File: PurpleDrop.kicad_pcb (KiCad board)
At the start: 4 copper layers, 213 x 141 mm, 118 parts, among them J1 Conn_02x32_Odd_Even, J2 Conn_02x32_Odd_Even, J3 Conn_02x20_Odd_Even, J4 Conn_01x04, J5 Conn_01x04, J6 Conn_01x04, J7 Conn_02x04_Odd_Even, J8 Conn_02x10_Odd_Even, J9 Barrel_Jack_Switch, Q1 SSM3K329R, Q2 SSM3K329R, Q3 SSM3K329R, Q4 SSM3K329R, U1 HV507, U10 RRE04EA6DFH, U11 RRE04EA6DFH, U12 RRE04EA6DFH, U13 RRE04EA6DFH, U14 RRE04EA6DFH, U15 RRE04EA6DFH, U16 RRE04EA6DFH, U17 RRE04EA6DFH, U18 RRE04EA6DFH, U19 RRE04EA6DFH, U2 HV507, U20 RRE04EA6DFH, U21 RRE04EA6DFH, U22 RRE04EA6DFH, U23 RRE04EA6DFH, U24 RRE04EA6DFH, U25 RRE04EA6DFH, U26 RRE04EA6DFH, U27 RRE04EA6DFH, U28 RRE04EA6DFH, U29 RRE04EA6DFH, U3 RRE04EA6DFH, U30 RRE04EA6DFH, U31 RRE04EA6DFH, U32 RRE04EA6DFH, U33 RRE04EA6DFH, U34 RRE04EA6DFH, U35 RRE04EA6DFH, U36 RRE04EA6DFH, U37 RRE04EA6DFH, U38 RRE04EA6DFH, U39 RRE04EA6DFH, U4 RRE04EA6DFH, U40 RRE04EA6DFH, U41 RRE04EA6DFH, U42 RRE04EA6DFH, U43 RRE04EA6DFH, U44 RRE04EA6DFH, U45 RRE04EA6DFH, U46 RRE04EA6DFH, U47 RRE04EA6DFH, U48 RRE04EA6DFH, U49 RRE04EA6DFH, U5 RRE04EA6DFH, U50 RRE04EA6DFH, U51 RRE04EA6DFH, U52 RRE04EA6DFH, U53 RRE04EA6DFH, U54 RRE04EA6DFH, U55 RRE04EA6DFH, U56 RRE04EA6DFH, U57 RRE04EA6DFH, U58 RRE04EA6DFH, U59 RRE04EA6DFH, U6 RRE04EA6DFH, U60 RRE04EA6DFH, U61 RRE04EA6DFH, U62 RRE04EA6DFH, U63 RRE04EA6DFH, U64 RRE04EA6DFH, U65 RRE04EA6DFH, U66 RRE04EA6DFH, U67 74LVC2T45DCT, U68 74LVC2T45DCT, U69 74LVC2T45DCT, U7 RRE04EA6DFH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

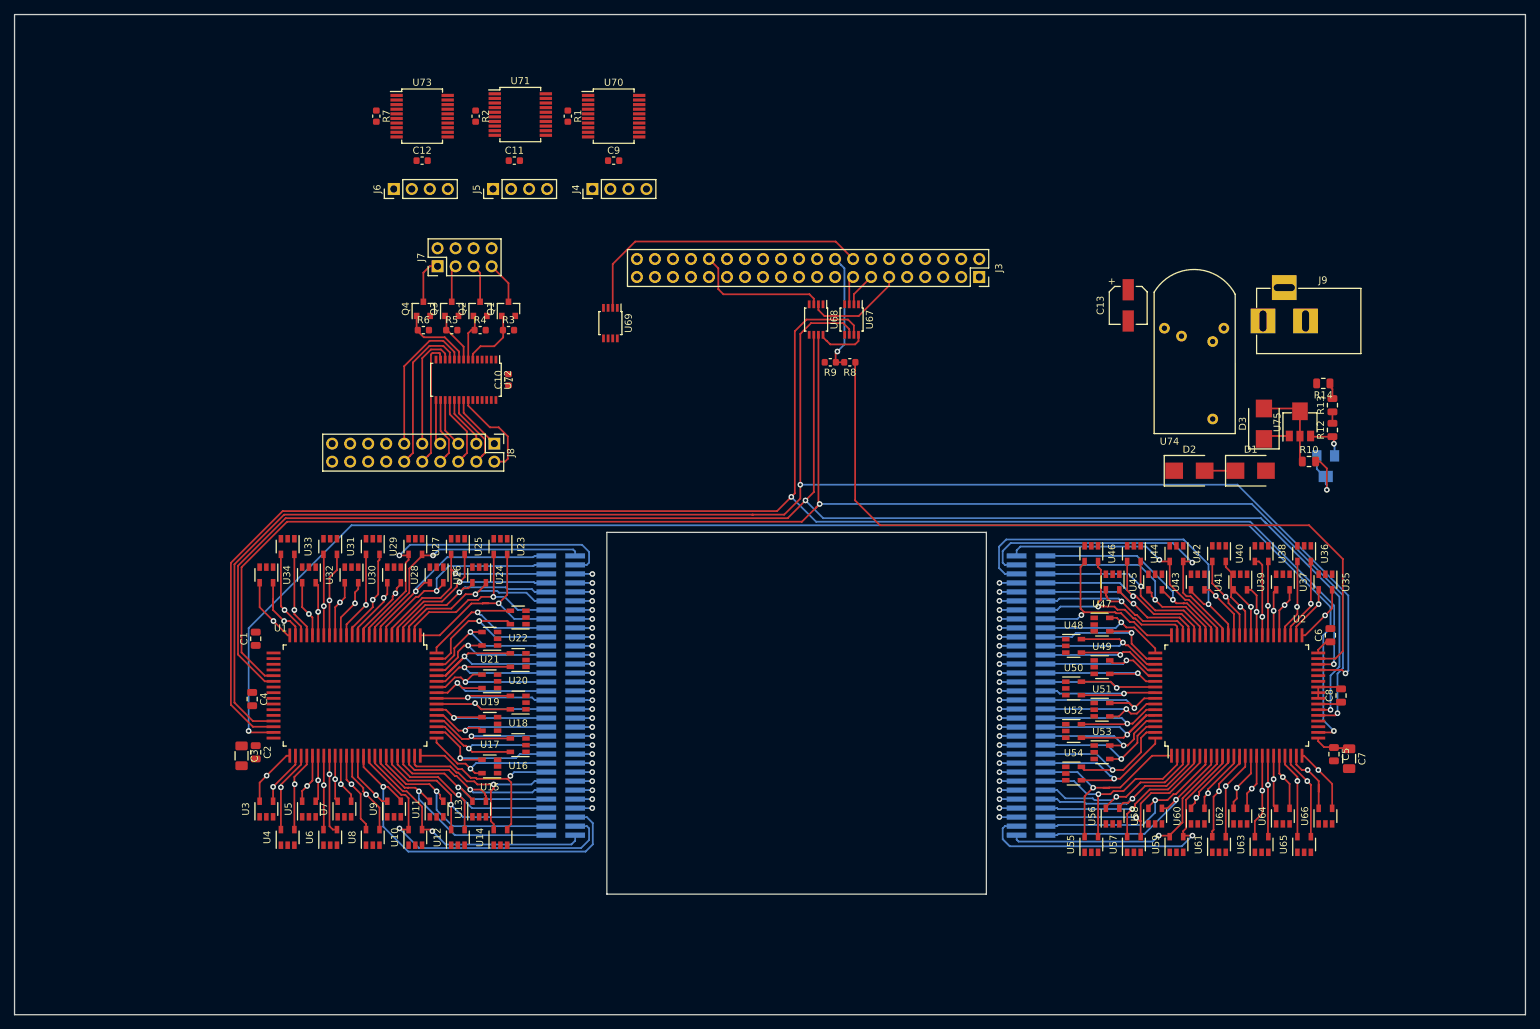
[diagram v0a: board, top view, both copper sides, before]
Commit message: feature complete.  need silk modifications
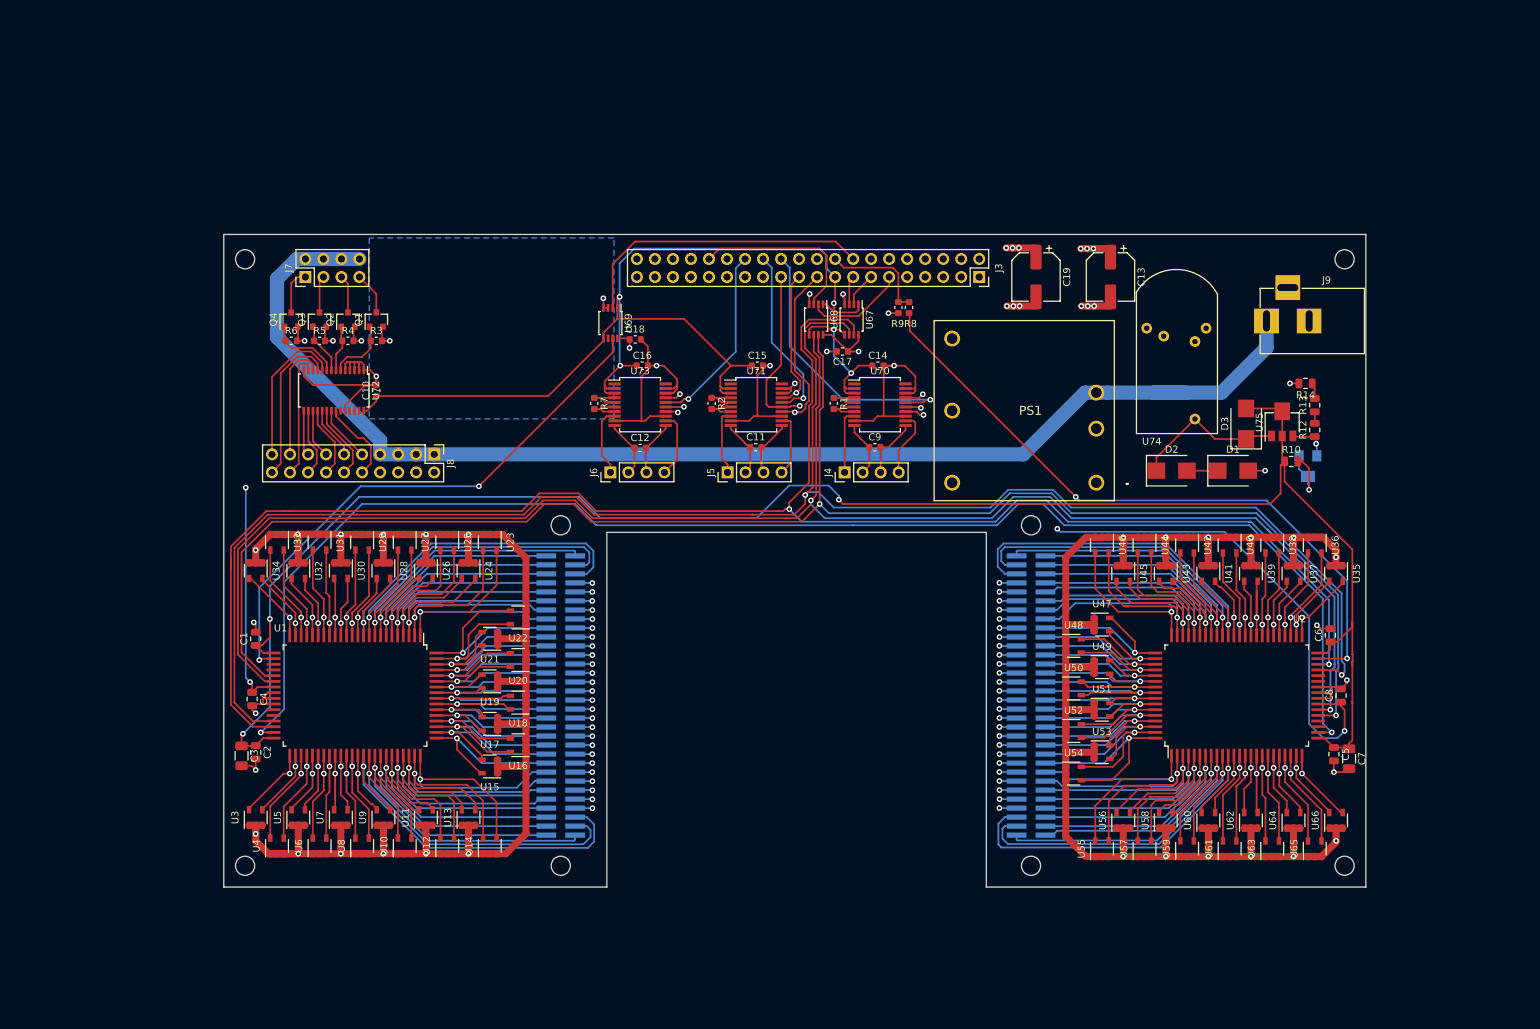
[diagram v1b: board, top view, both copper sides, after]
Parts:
- added C14: 0.1uF, Capacitor_SMD:C_0603_1608Metric, F.Cu at (164.7, 73.5)
- added C15: 0.1uF, Capacitor_SMD:C_0603_1608Metric, F.Cu at (147.7, 73.5)
- added C16: 0.1uF, Capacitor_SMD:C_0603_1608Metric, F.Cu at (131.5, 73.5)
- added C17: 0.1uF, Capacitor_SMD:C_0603_1608Metric, F.Cu at (159.7, 71.5)
- added C18: 0.1uF, Capacitor_SMD:C_0603_1608Metric, F.Cu at (130.5, 69.8)
- added C19: 100uF, Capacitor_SMD:CP_Elec_6.3x5.9, F.Cu at (187.0, 61.0)
- added PS1: PDQE15-Q24-S5-D, CUI:PDQE15Q24S5D, F.Cu at (195.5, 90.0)
- added REF**: MountingHole_2.7mm_M2.5_ISO14580, MountingHole:MountingHole_2.7mm_M2.5_ISO14580, F.Cu at (186.3, 96.0)
- added REF**: MountingHole_2.7mm_M2.5_ISO14580, MountingHole:MountingHole_2.7mm_M2.5_ISO14580, F.Cu at (120.0, 96.0)
- added REF**: MountingHole_2.7mm_M2.5_ISO14580, MountingHole:MountingHole_2.7mm_M2.5_ISO14580, F.Cu at (230.5, 58.5)
- added REF**: MountingHole_2.7mm_M2.5_ISO14580, MountingHole:MountingHole_2.7mm_M2.5_ISO14580, F.Cu at (75.5, 58.5)
- added REF**: MountingHole_2.7mm_M2.5_ISO14580, MountingHole:MountingHole_2.7mm_M2.5_ISO14580, F.Cu at (230.5, 144.0)
- added REF**: MountingHole_2.7mm_M2.5_ISO14580, MountingHole:MountingHole_2.7mm_M2.5_ISO14580, F.Cu at (186.3, 144.0)
- added REF**: MountingHole_2.7mm_M2.5_ISO14580, MountingHole:MountingHole_2.7mm_M2.5_ISO14580, F.Cu at (120.0, 144.0)
- added REF**: MountingHole_2.7mm_M2.5_ISO14580, MountingHole:MountingHole_2.7mm_M2.5_ISO14580, F.Cu at (75.5, 144.0)
- added Ref**: Val**, logos:purpledrop, B.Cu at (110.5, 75.0)
- added Ref**: Val**, logos:wlogo, B.Cu at (121.0, 62.0)
- added Ref**: Val**, logos:misl-logo, B.Cu at (109.0, 55.0)
- C13: value 47uF -> 100uF; footprint Capacitor_SMD:CP_Elec_5x5.8 -> Capacitor_SMD:CP_Elec_6.3x5.9
- moved U70 55.4 mm to (165.0, 79.0)
- moved R1 55.2 mm to (158.5, 78.8)
- moved C9 54.7 mm to (164.3, 85.0)
- moved J4 53.5 mm to (160.0, 88.5)
- moved C11 52.8 mm to (147.5, 85.0)
- moved U71 52.7 mm to (147.6, 79.0)
- moved R2 52.4 mm to (141.3, 78.8)
- moved J5 51.8 mm to (143.5, 88.5)
- moved U73 51.0 mm to (131.2, 79.0)
- moved C12 50.8 mm to (131.2, 85.1)
- moved R7 50.8 mm to (124.7, 78.8)
- moved J6 50.3 mm to (127.0, 88.5)
- moved C10 18.7 mm to (94.0, 77.0)
- moved J7 18.7 mm to (84.0, 61.0)
- moved Q1 18.7 mm to (94.0, 67.0)
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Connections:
- J3 pad 1: +3V3 -> Net-(J3-Pad1)
- J3 pad 17: Net-(J3-Pad17) -> +3V3
- J3 pad 20: Net-(J3-Pad20) -> GND
- J3 pad 25: Net-(J3-Pad25) -> GND
- J3 pad 30: Net-(J3-Pad30) -> GND
- J3 pad 34: Net-(J3-Pad34) -> GND
- J3 pad 39: Net-(J3-Pad39) -> GND
- J3 pad 9: Net-(J3-Pad9) -> GND
- J8 pad 1: /peripherals/PWM14 -> +12V
- J8 pad 10: /peripherals/PWM7 -> /peripherals/PWM15
- J8 pad 11: /peripherals/PWM4 -> /peripherals/PWM12
- J8 pad 12: /peripherals/PWM5 -> /peripherals/PWM13
- J8 pad 13: +12V -> /peripherals/PWM10
- J8 pad 14: GND -> /peripherals/PWM11
- J8 pad 15: +12V -> /peripherals/PWM8
- J8 pad 16: GND -> /peripherals/PWM9
- J8 pad 17: +12V -> /peripherals/PWM6
- J8 pad 18: GND -> /peripherals/PWM7
- J8 pad 19: +12V -> /peripherals/PWM4
- J8 pad 2: /peripherals/PWM15 -> GND
- J8 pad 20: GND -> /peripherals/PWM5
- J8 pad 3: /peripherals/PWM12 -> +12V
- J8 pad 4: /peripherals/PWM13 -> GND
- J8 pad 5: /peripherals/PWM10 -> +12V
- J8 pad 6: /peripherals/PWM11 -> GND
- J8 pad 7: /peripherals/PWM8 -> +12V
- J8 pad 8: /peripherals/PWM9 -> GND
- J8 pad 9: /peripherals/PWM6 -> /peripherals/PWM14
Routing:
- net GND: track 4.90 -> 599.6 mm, vias 0 -> 52
- net V_HV: track 20.3 -> 265.3 mm, vias 0 -> 3
- net +12V: track 0.00 -> 189.8 mm, vias 0 -> 3
- net +3V3: track 0.00 -> 172.2 mm, vias 0 -> 5
- net +5V: track 10.1 -> 118.3 mm, vias 0 -> 9
- net HV_DIN: track 0.00 -> 78.7 mm, vias 0 -> 2
- net pi_MOSI_0: track 0.00 -> 63.7 mm, vias 0 -> 3
- net pi_SCK_0: track 0.00 -> 62.2 mm, vias 0 -> 3
- net pi_MISO_0: track 0.00 -> 59.2 mm, vias 0 -> 3
- net pi_CE0_0: track 0.00 -> 39.4 mm, vias 0 -> 1
- net pi_CE2_sw: track 0.00 -> 26.5 mm, vias 0 -> 1
- net pi_CE1_0: track 0.00 -> 25.3 mm, vias 0 -> 1
- net Net-(D2-Pad1): track 3.76 -> 21.7 mm
- net HV_DOUT: track 108.5 -> 93.8 mm, vias 0 -> 2
- net /HV interface/HVOUT2_23: track 27.9 -> 41.7 mm
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- added copper zone on B.Cu, net (none)
- added copper zone on In2.Cu, net +12V
- added copper zone on In2.Cu, net +5V
- added copper zone on In1.Cu, net GND
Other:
- board size 213 x 141 mm -> 161 x 92 mm
- board text added: "TODO: HV power switch isolate 5v switcher if plug not present"
- board text added: "v0.5.0"

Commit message: complete.  needs small anotation cleanup and testpoints
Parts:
- added C20: 1uf 450v, Capacitor_SMD:CP_Elec_8x10, F.Cu at (220.8, 76.0)
- added R15: 10k, Resistor_SMD:R_0603_1608Metric, F.Cu at (214.8, 61.1)
- added SW1: SW_SPDT, TECON:1825232-1, F.Cu at (214.3, 57.5)
- moved R14 6.25 mm to (229.8, 80.0), turned to 90 degrees
- moved D3 5.70 mm to (220.1, 86.2)
- moved R10 5.70 mm to (226.5, 91.5)
- moved R12 5.70 mm to (229.8, 87.1)
- moved R13 5.70 mm to (229.8, 83.6)
- moved U75 5.70 mm to (225.2, 86.4)
- moved R11 3.23 mm to (228.0, 89.5)
- moved D1 2.50 mm to (212.3, 88.3)
- moved D2 2.00 mm to (204.1, 88.3)
- moved J9 1.20 mm to (219.5, 66.0)
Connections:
- U74 pad 5: +12V -> Net-(R15-Pad2)
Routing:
- net +5V: track 118.3 -> 25.6 mm, vias 9 -> 7
- net Net-(R15-Pad2): track 0.00 -> 19.0 mm
- net Net-(D2-Pad1): track 21.7 -> 29.4 mm
- net GND: track 599.6 -> 606.0 mm, vias 52 -> 55
- net +12V: track 189.8 -> 185.7 mm
- net Net-(R10-Pad2): track 10.5 -> 6.78 mm
- net V_HV: track 265.3 -> 266.9 mm
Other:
- board text added: "+"
- board text added: "+12v"
- board text added: "+V5"
- board text added: "-"
- board text added: "0"
- board text added: "1"
- board text added: "10"
- board text added: "11"
- board text added: "12"
- board text added: "13"
- board text added: "14"
- board text added: "15"
- board text added: "2"
- board text added: "3"
- board text added: "4"
- board text added: "5"
- board text added: "6"
- board text added: "7"
- board text added: "8"
- board text added: "9"
- board text added: "CTRL"
- board text added: "GND"
- board text added: "HEAT"
- board text added: "HV ADJUST"
- board text added: "HV OFF"
- board text added: "HV ON"
- board text added: "PWM"
- board text added: "RTD0"
- board text added: "RTD1"
- board text added: "RTD2"
- board text added: "TODO: add 5v pwr switch? add test points"
- board text added: "TRIM"
- board text removed: "TODO: HV power switch isolate 5v switcher if plug not present"

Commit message: version sent to fab
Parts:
- added D4: LED_Small, LED_SMD:LED_0805_2012Metric, B.Cu at (206.9, 59.9)
- added R16: 10k, Resistor_SMD:R_0603_1608Metric, B.Cu at (210.4, 59.9)
- added TP1: TestPoint_Alt, TestPoint:TestPoint_Keystone_5000-5004_Miniature, F.Cu at (114.2, 93.3)
- added TP2: TestPoint_Alt, TestPoint:TestPoint_Keystone_5000-5004_Miniature, F.Cu at (108.5, 89.2)
- added TP3: TestPoint_Alt, TestPoint:TestPoint_Keystone_5000-5004_Miniature, F.Cu at (230.0, 95.7)
- added TP4: TestPoint_Alt, TestPoint:TestPoint_Keystone_5000-5004_Miniature, F.Cu at (229.8, 76.3)
- moved C2 2.02 mm to (79.0, 128.3)
- moved C3 2.02 mm to (77.0, 128.8)
- moved C5 2.00 mm to (227.0, 128.3)
- moved C7 2.00 mm to (229.1, 128.9)
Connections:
- SW1 pad GND: GND -> (no net)
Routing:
- net Net-(R15-Pad2): track 19.0 -> 22.4 mm
- net GND: track 606.0 -> 608.3 mm
- net Net-(D4-Pad2): track 0.00 -> 1.76 mm
- net DIO_CASCADE: track 204.7 -> 205.9 mm
- net V_HV: track 266.9 -> 266.2 mm
- net HV_DIN: track 78.7 -> 78.8 mm, vias 2 -> 1
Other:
- board text added: "16 15 14 13 12 11 10 09 08 07 06 05 04 03 02 01 64 63 62 61 60 59 58 57 56 55 54 53 52 51 50 49"
- board text added: "17 18 19 20 21 22 23 24 25 26 27 28 29 30 31 32 33 34 35 36 37 38 39 40 41 42 43 44 45 46 47 48"
- board text added: "48 47 46 45 44 43 42 41 40 39 38 37 36 35 34 33 32 31 30 29 28 27 26 25 24 23 22 21 20 19 18 17"
- board text added: "49 50 51 52 53 54 55 56 57 58 59 60 61 62 63 64 01 02 03 04 05 06 07 08 09 10 11 12 13 14 15 16"
- board text added: "BL"
- board text added: "CLK"
- board text added: "HV CLK"
- board text added: "HV DIN"
- board text added: "HV1"
- board text added: "HV2"
- board text added: "LE"
- board text added: "POL"
- board text added: "V_HV"
- board text removed: "TODO: add 5v pwr switch? add test points"

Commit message: informational updates and minor sinkscreen tweak
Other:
- board text added: "v0.5.1"
- board text removed: "v0.5.0"
